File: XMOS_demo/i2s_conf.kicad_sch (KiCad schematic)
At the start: 12 parts, among them J10 Conn_PMOD_02x06, J11 Conn_PMOD_02x06

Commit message: Summary (required)
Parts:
- renumbered JP6 to JP2, JP2 to JP3, JP7 to JP4, JP3 to JP5, JP8 to JP6, JP4 to JP7, JP9 to JP8, JP5 to JP9
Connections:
- net I2S_ADC_PMOD1: now also J10.3 (Pin_3)
- net I2S_ADC_PMOD2: now also J11.3 (Pin_3)
- net I2S_DAC_PMOD1: now also J10.2 (Pin_2)
- net I2S_DAC_PMOD2: now also J11.2 (Pin_2)
- net I2S_LRCK_PMOD1: now also J10.1 (Pin_1)
- net I2S_LRCK_PMOD2: now also J11.1 (Pin_1)
- net I2S_SCLK_PMOD1: now also J10.4 (Pin_4)
- net I2S_SCLK_PMOD2: now also J11.4 (Pin_4)
- net MCLK_PMOD1: now also J10.9 (Pin_9)
- net MCLK_PMOD2: now also J11.9 (Pin_9)
- net GND: now reaches J10.11 (Pin_11)
- net GND: now also J10.5 (Pin_5), J11.11 (Pin_11), J11.5 (Pin_5)
- no-connect marks 0 -> 10
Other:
- note added: "I2S - Codec"
- note added: "I2S - DSP"
- note added: "I2S - FPGA (PMOD connectors)"
- note removed: "I2S From DSP"
- note removed: "I2S To Codec"
- moved on the sheet: J10, J11

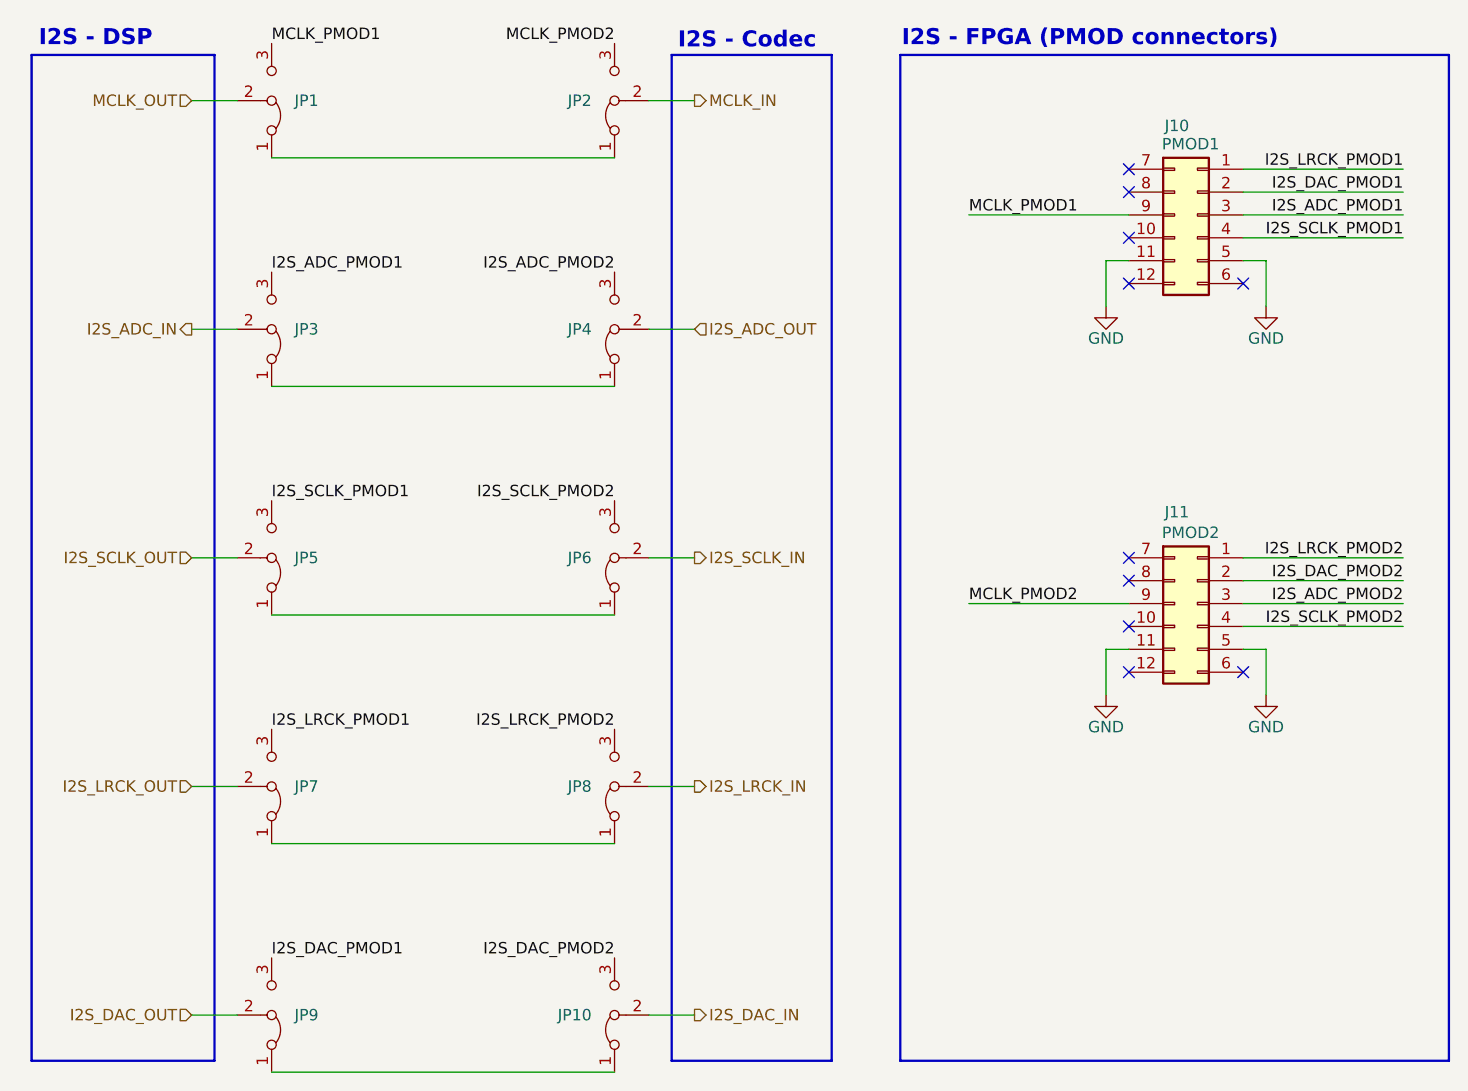
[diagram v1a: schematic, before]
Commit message: Started changes on power supply (audio in) on schematic
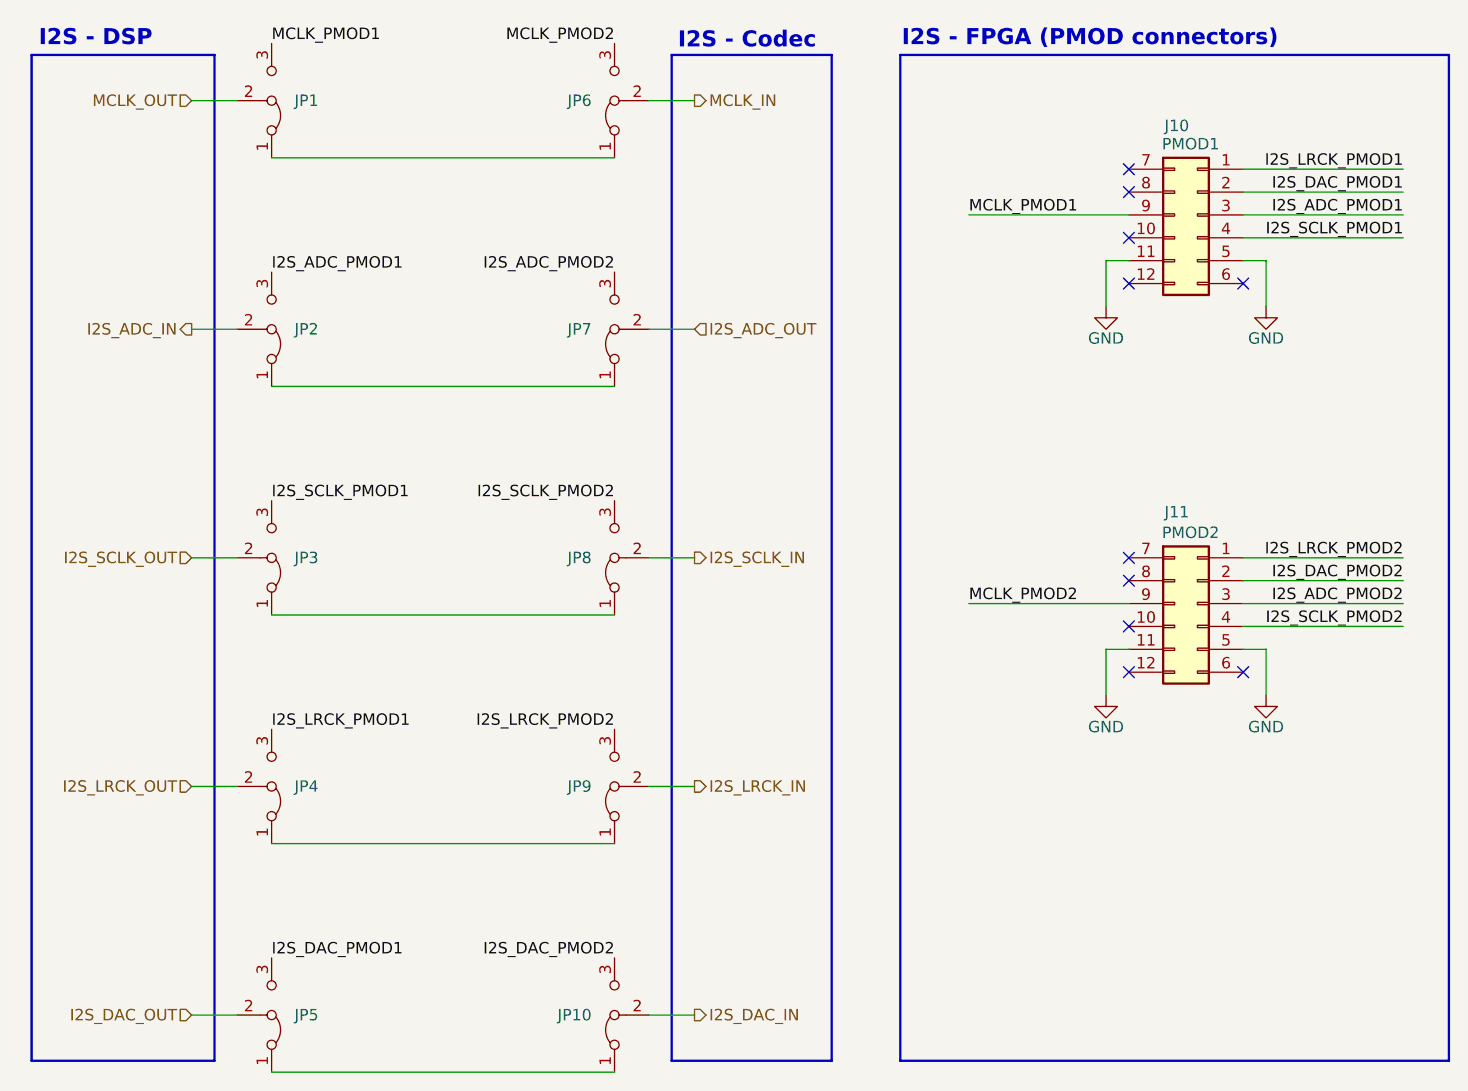
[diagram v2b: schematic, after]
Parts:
- renumbered JP3 to JP2, JP5 to JP3, JP7 to JP4, JP9 to JP5, JP2 to JP6, JP4 to JP7, JP6 to JP8, JP8 to JP9
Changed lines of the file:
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@@
 		(on_board yes)
 		(dnp no)
-		(property "Reference" "JP5"
+		(property "Reference" "JP3"
 			(at 85.09 101.6001 90)
 			(effects
@@
 			(project "XMOS_demo"
 				(path "/0a855fb0-ca19-4770-811e-70d8770d7fdd/743d39d7-addd-4319-9e96-2bb2c2d7c5c3"
-					(reference "JP5")
+					(reference "JP3")
 					(unit 1)
 				)
@@
 		(on_board yes)
 		(dnp no)
-		(property "Reference" "JP4"
+		(property "Reference" "JP7"
 			(at 118.11 76.2001 90)
 			(effects
@@
 			(project "XMOS_demo"
 				(path "/0a855fb0-ca19-4770-811e-70d8770d7fdd/743d39d7-addd-4319-9e96-2bb2c2d7c5c3"
-					(reference "JP4")
+					(reference "JP7")
 					(unit 1)
 				)
@@
 		(on_board yes)
 		(dnp no)
-		(property "Reference" "JP9"
+		(property "Reference" "JP5"
 			(at 85.09 152.4001 90)
 			(effects
@@
 			(project "XMOS_demo"
 				(path "/0a855fb0-ca19-4770-811e-70d8770d7fdd/743d39d7-addd-4319-9e96-2bb2c2d7c5c3"
-					(reference "JP9")
+					(reference "JP5")
 					(unit 1)
 				)
@@
 		(on_board yes)
 		(dnp no)
-		(property "Reference" "JP7"
+		(property "Reference" "JP4"
 			(at 85.09 127.0001 90)
 			(effects
@@
 			(project "XMOS_demo"
 				(path "/0a855fb0-ca19-4770-811e-70d8770d7fdd/743d39d7-addd-4319-9e96-2bb2c2d7c5c3"
-					(reference "JP7")
+					(reference "JP4")
 					(unit 1)
 				)
@@
 		(on_board yes)
 		(dnp no)
-		(property "Reference" "JP2"
+		(property "Reference" "JP6"
 			(at 118.11 50.8001 90)
 			(effects
@@
 			(project "XMOS_demo"
 				(path "/0a855fb0-ca19-4770-811e-70d8770d7fdd/743d39d7-addd-4319-9e96-2bb2c2d7c5c3"
-					(reference "JP2")
+					(reference "JP6")
 					(unit 1)
 				)
@@
 		(on_board yes)
 		(dnp no)
-		(property "Reference" "JP3"
+		(property "Reference" "JP2"
 			(at 85.09 76.2001 90)
 			(effects
@@
 			(project "XMOS_demo"
 				(path "/0a855fb0-ca19-4770-811e-70d8770d7fdd/743d39d7-addd-4319-9e96-2bb2c2d7c5c3"
-					(reference "JP3")
+					(reference "JP2")
 					(unit 1)
 				)
@@
 		(on_board yes)
 		(dnp no)
-		(property "Reference" "#PWR0102"
+		(property "Reference" "#PWR0101"
 			(at 175.26 123.19 0)
 			(effects
@@
 			(project "XMOS_demo"
 				(path "/0a855fb0-ca19-4770-811e-70d8770d7fdd/743d39d7-addd-4319-9e96-2bb2c2d7c5c3"
-					(reference "#PWR0102")
+					(reference "#PWR0101")
 					(unit 1)
 				)
@@
 		(on_board yes)
 		(dnp no)
-		(property "Reference" "JP8"
+		(property "Reference" "JP9"
 			(at 118.11 127.0001 90)
 			(effects
@@
 			(project "XMOS_demo"
 				(path "/0a855fb0-ca19-4770-811e-70d8770d7fdd/743d39d7-addd-4319-9e96-2bb2c2d7c5c3"
-					(reference "JP8")
+					(reference "JP9")
 					(unit 1)
 				)
@@
 		(on_board yes)
 		(dnp no)
-		(property "Reference" "#PWR0101"
+		(property "Reference" "#PWR0102"
 			(at 193.04 80.01 0)
 			(effects
@@
 			(project "XMOS_demo"
 				(path "/0a855fb0-ca19-4770-811e-70d8770d7fdd/743d39d7-addd-4319-9e96-2bb2c2d7c5c3"
-					(reference "#PWR0101")
+					(reference "#PWR0102")
 					(unit 1)
 				)
@@
 		(on_board yes)
 		(dnp no)
-		(property "Reference" "JP6"
+		(property "Reference" "JP8"
 			(at 118.11 101.6001 90)
 			(effects
@@
 			(project "XMOS_demo"
 				(path "/0a855fb0-ca19-4770-811e-70d8770d7fdd/743d39d7-addd-4319-9e96-2bb2c2d7c5c3"
-					(reference "JP6")
-					(unit 1)
-				)
+					(reference "JP8")
+					(unit 1)
+				)

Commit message: Passive lpf added to autio output
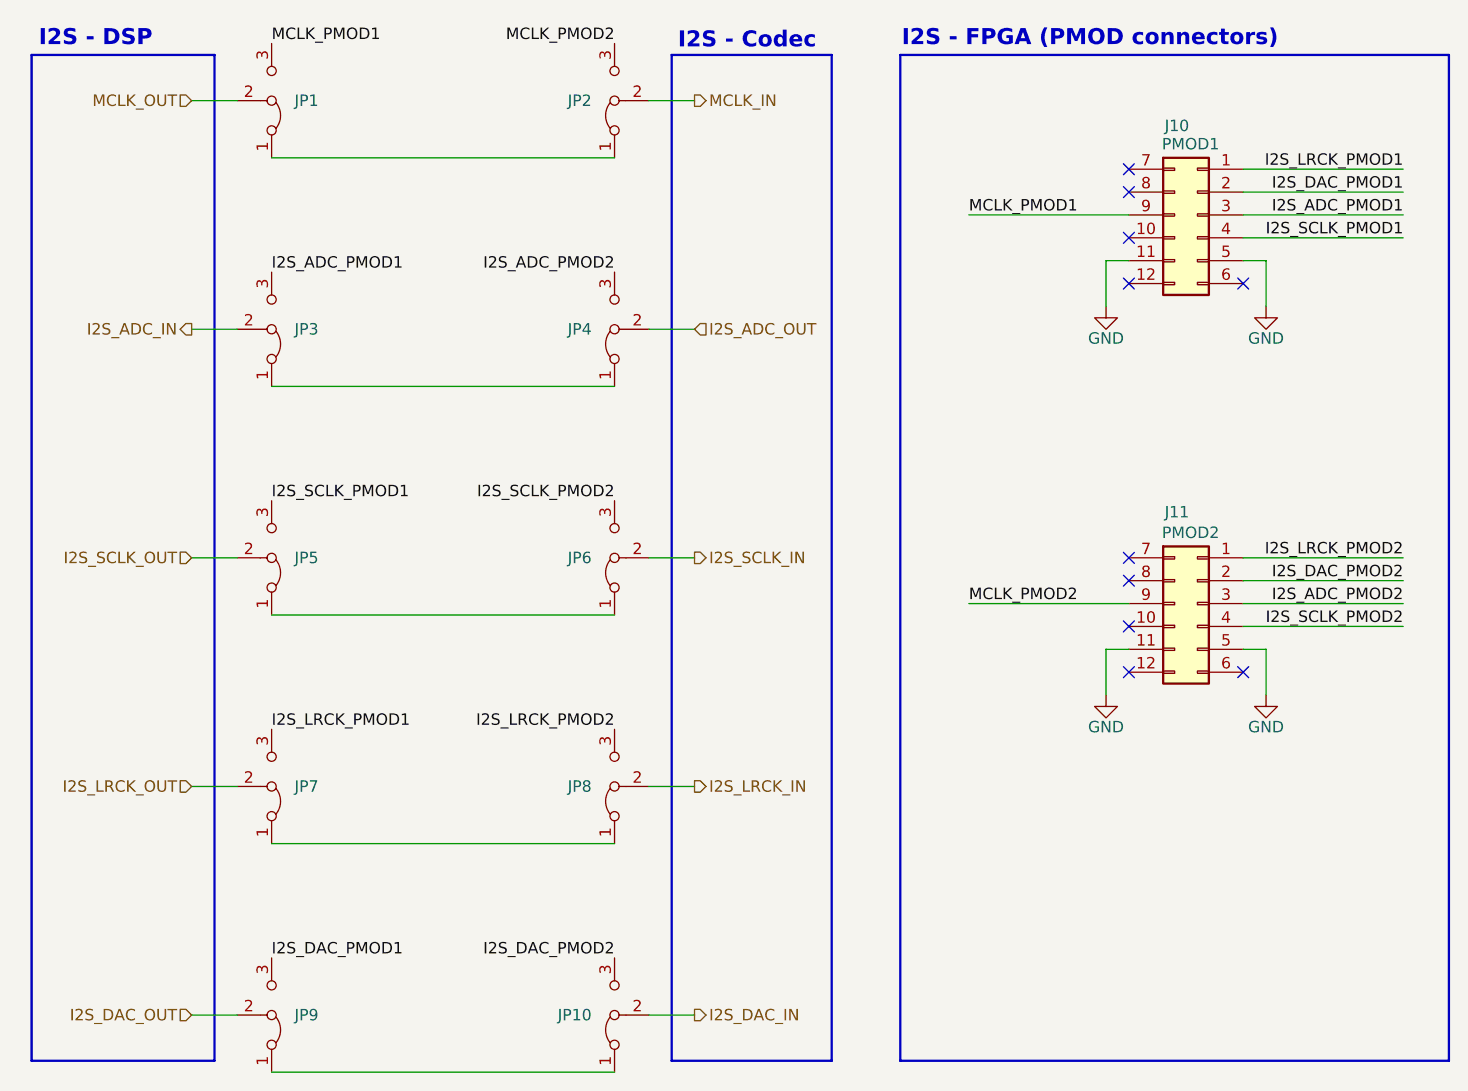
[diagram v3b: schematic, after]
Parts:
- renumbered JP6 to JP2, JP2 to JP3, JP7 to JP4, JP3 to JP5, JP8 to JP6, JP4 to JP7, JP9 to JP8, JP5 to JP9
